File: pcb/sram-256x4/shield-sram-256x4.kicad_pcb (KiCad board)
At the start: 4 copper layers, 100 x 100 mm, 26 parts, among them J1 QSH-060-01-L-D-A, J2 QSH-060-01-L-D-A, U1 IS61WV25616-10TLI, U2 IS61WV25616-10TLI, U3 IS61WV25616-10TLI, U4 IS61WV25616-10TLI

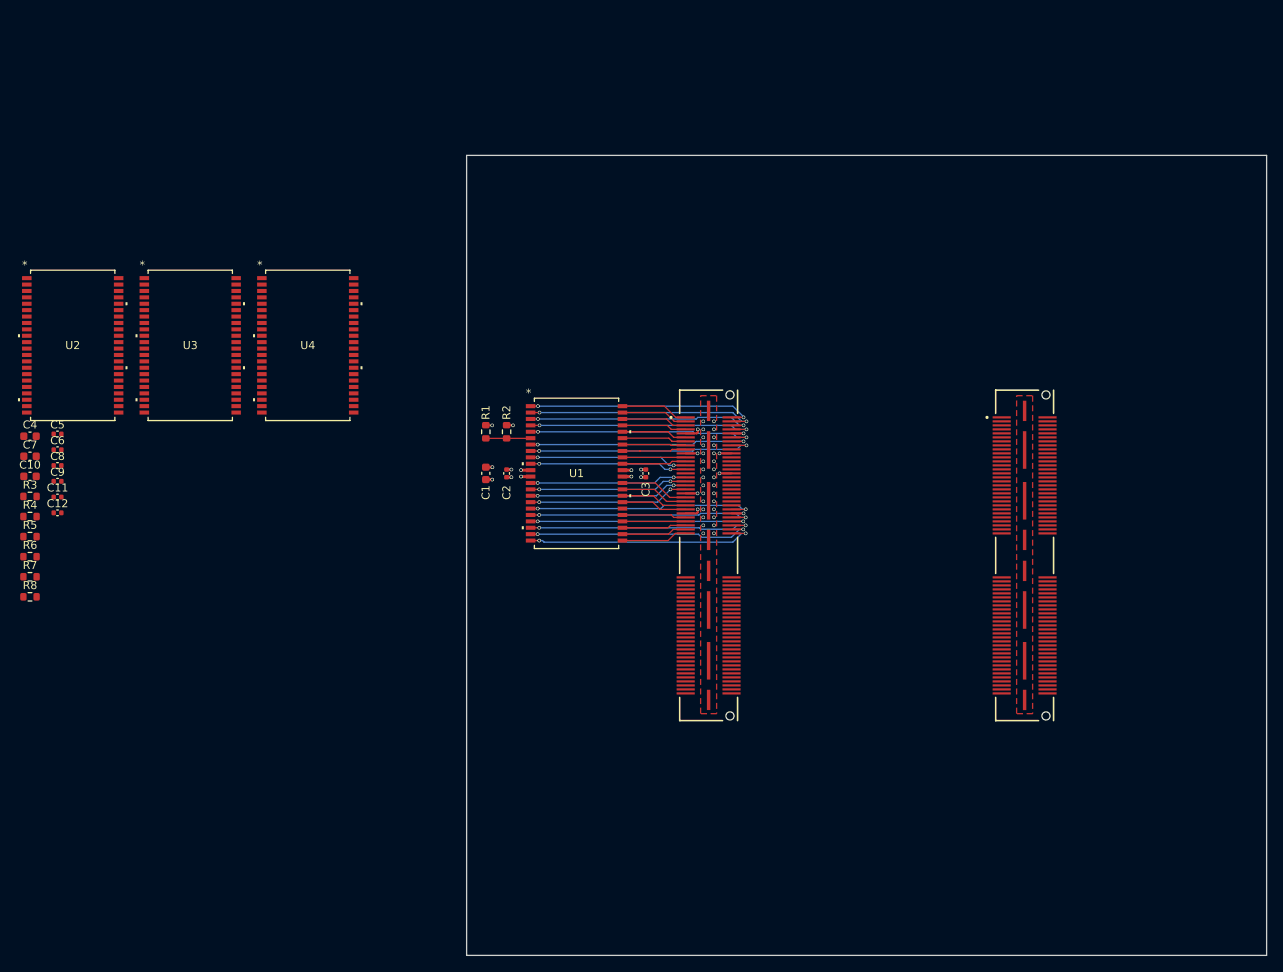
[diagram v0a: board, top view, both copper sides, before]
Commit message: [pcb][sram-4x] all but pmod routed for adc board
The sram is doing double duty here during the cross over. It supports
the dfc stacking connector during the transition. It will be removed.
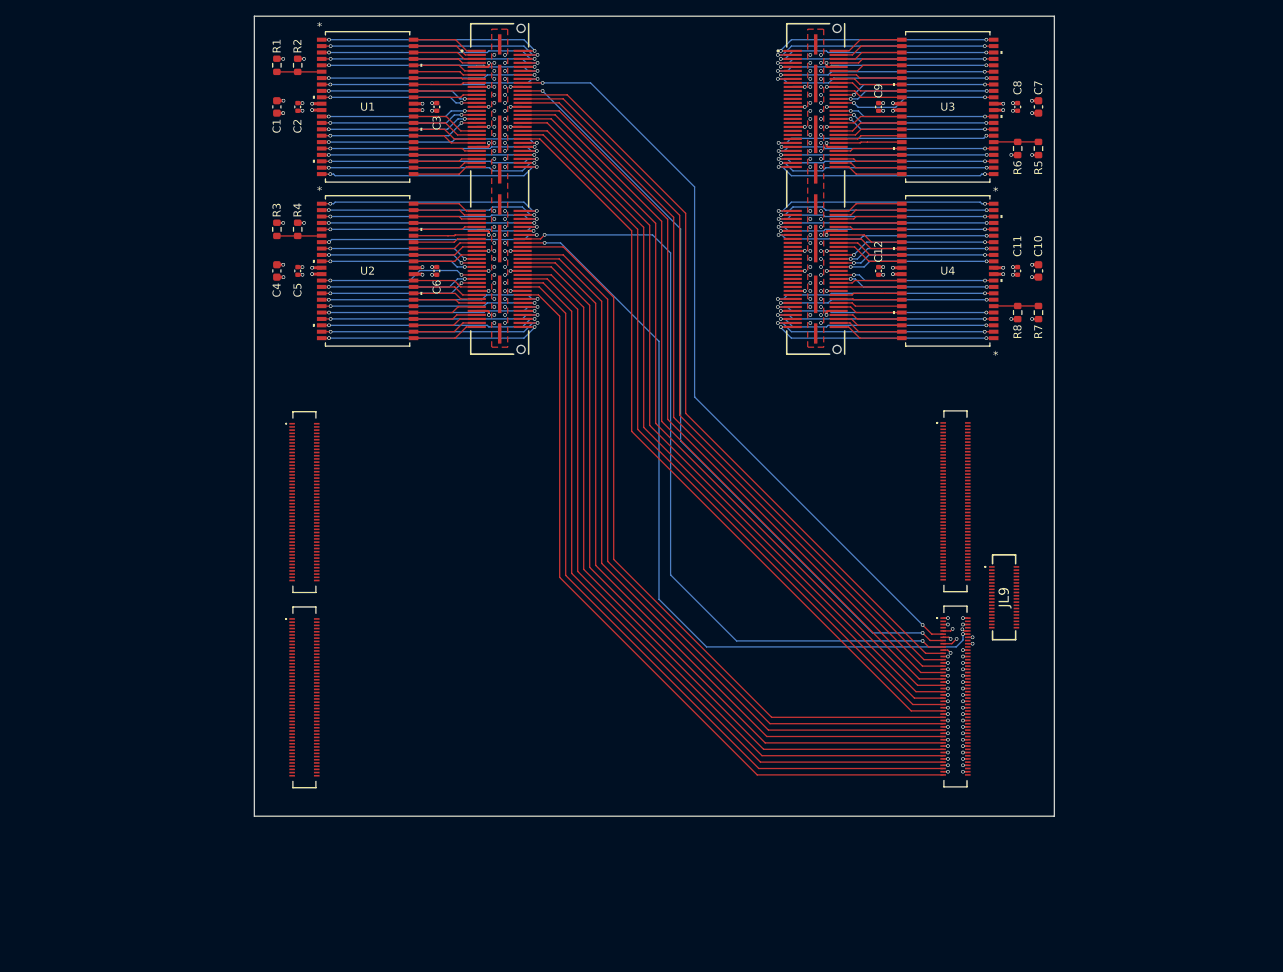
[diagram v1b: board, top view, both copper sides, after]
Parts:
- added JL1: DF40C-100DS-0.4V51, DF40C-100DS-0.4V_51:DF40C100DS04V51, F.Cu at (37.5, 90.9)
- added JL2: DF40C-100DS-0.4V51, DF40C-100DS-0.4V_51:DF40C100DS04V51, F.Cu at (37.5, 115.3)
- added JL3: DF40C-100DS-0.4V51, DF40C-100DS-0.4V_51:DF40C100DS04V51, F.Cu at (118.9, 90.8)
- added JL4: DF40C-100DS-0.4V51, DF40C-100DS-0.4V_51:DF40C100DS04V51, F.Cu at (118.9, 115.2)
- added JL9: DF40C-40DS-0.4V51, DF40C-40DS-0.4V_51:DF40C40DS04V51, F.Cu at (125.0, 102.8)
- moved R5 135.1 mm to (129.3, 46.7), turned to 90 degrees
- moved R6 133.6 mm to (126.7, 46.7), turned to 90 degrees
- moved C7 133.4 mm to (129.3, 41.5), turned to 90 degrees
- moved R7 130.3 mm to (129.3, 67.2), turned to 90 degrees
- moved C10 128.6 mm to (129.3, 62.0), turned to 90 degrees
- moved R8 128.5 mm to (126.7, 67.2), turned to 90 degrees
- moved C8 128.1 mm to (126.7, 41.5), turned to 90 degrees
- moved C11 123.3 mm to (126.7, 62.0), turned to 90 degrees
- moved C9 112.8 mm to (109.3, 41.5), turned to -90 degrees
- moved C12 107.0 mm to (109.3, 62.0), turned to -90 degrees
- moved U3 99.3 mm to (117.9, 41.5), turned to 180 degrees
- moved U4 80.5 mm to (117.9, 62.0), turned to 180 degrees
- moved J2 52.7 mm to (101.4, 51.8)
- moved U1 52.7 mm to (45.4, 41.5)
- moved C1 52.7 mm to (34.1, 41.5)
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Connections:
- R6 pad 1: /U3_CEn -> GND
- R6 pad 2: GND -> /U3_CEn
- R8 pad 1: /U4_CEn -> GND
- R8 pad 2: GND -> /U4_CEn
- U2 pad 10: B23 -> B25
- U2 pad 13: B25 -> B27
- U2 pad 14: B27 -> B29
- U2 pad 15: B29 -> B31
- U2 pad 16: B31 -> B38
- U2 pad 35: B15 -> B19
- U2 pad 36: B13 -> B17
- U2 pad 37: B11 -> B15
- U2 pad 38: B9 -> B13
- U2 pad 39: GND -> B11
- U2 pad 40: GND -> B9
- U2 pad 7: B17 -> B12
- U2 pad 8: B19 -> B21
- U2 pad 9: B21 -> B23
- U3 pad 1: unconnected-(U3-A0-Pad1) -> C49
- U3 pad 10: unconnected-(U3-I/O3-Pad10) -> C26
- U3 pad 13: unconnected-(U3-I/O4-Pad13) -> C24
- U3 pad 14: unconnected-(U3-I/O5-Pad14) -> C22
- U3 pad 15: unconnected-(U3-I/O6-Pad15) -> C20
- U3 pad 16: unconnected-(U3-I/O7-Pad16) -> C13
- U3 pad 17: unconnected-(U3-WE-Pad17) -> C11
- U3 pad 18: unconnected-(U3-A5-Pad18) -> C9
- U3 pad 19: unconnected-(U3-A6-Pad19) -> C7
- U3 pad 2: unconnected-(U3-A1-Pad2) -> C47
- U3 pad 20: unconnected-(U3-A7-Pad20) -> C5
- U3 pad 21: unconnected-(U3-A8-Pad21) -> C3
- U3 pad 22: unconnected-(U3-A9-Pad22) -> C1
- U3 pad 23: unconnected-(U3-A10-Pad23) -> C2
- U3 pad 24: unconnected-(U3-A11-Pad24) -> C4
- U3 pad 25: unconnected-(U3-A12-Pad25) -> C6
- U3 pad 26: unconnected-(U3-A13-Pad26) -> C8
- U3 pad 27: unconnected-(U3-A14-Pad27) -> C10
- U3 pad 29: unconnected-(U3-I/O8-Pad29) -> C12
- U3 pad 3: unconnected-(U3-A2-Pad3) -> C45
- U3 pad 30: unconnected-(U3-I/O9-Pad30) -> C14
- U3 pad 31: unconnected-(U3-I/O10-Pad31) -> C16
- U3 pad 32: unconnected-(U3-I/O11-Pad32) -> C18
- U3 pad 35: unconnected-(U3-I/O12-Pad35) -> C32
- U3 pad 36: unconnected-(U3-I/O13-Pad36) -> C34
- U3 pad 37: unconnected-(U3-I/O14-Pad37) -> C36
- U3 pad 38: unconnected-(U3-I/O15-Pad38) -> C38
- U3 pad 39: GND -> C40
- U3 pad 4: unconnected-(U3-A3-Pad4) -> C43
- U3 pad 40: GND -> C42
- U3 pad 41: unconnected-(U3-OE-Pad41) -> C44
- U3 pad 42: unconnected-(U3-A15-Pad42) -> C46
- U3 pad 43: unconnected-(U3-A16-Pad43) -> C48
- U3 pad 44: unconnected-(U3-A17-Pad44) -> C50
- U3 pad 5: unconnected-(U3-A4-Pad5) -> C41
- U3 pad 7: unconnected-(U3-I/O0-Pad7) -> C39
- U3 pad 8: unconnected-(U3-I/O1-Pad8) -> C30
- U3 pad 9: unconnected-(U3-I/O2-Pad9) -> C28
- U4 pad 1: unconnected-(U4-A0-Pad1) -> D49
- U4 pad 10: unconnected-(U4-I/O3-Pad10) -> D28
- U4 pad 13: unconnected-(U4-I/O4-Pad13) -> D26
- U4 pad 14: unconnected-(U4-I/O5-Pad14) -> D24
- U4 pad 15: unconnected-(U4-I/O6-Pad15) -> D22
- U4 pad 16: unconnected-(U4-I/O7-Pad16) -> D20
- U4 pad 17: unconnected-(U4-WE-Pad17) -> D11
- U4 pad 18: unconnected-(U4-A5-Pad18) -> D9
- U4 pad 19: unconnected-(U4-A6-Pad19) -> D7
- U4 pad 2: unconnected-(U4-A1-Pad2) -> D47
- U4 pad 20: unconnected-(U4-A7-Pad20) -> D5
- U4 pad 21: unconnected-(U4-A8-Pad21) -> D3
- U4 pad 22: unconnected-(U4-A9-Pad22) -> D1
- U4 pad 23: unconnected-(U4-A10-Pad23) -> D2
- U4 pad 24: unconnected-(U4-A11-Pad24) -> D4
- U4 pad 25: unconnected-(U4-A12-Pad25) -> D6
- U4 pad 26: unconnected-(U4-A13-Pad26) -> D8
- U4 pad 27: unconnected-(U4-A14-Pad27) -> D10
- U4 pad 29: unconnected-(U4-I/O8-Pad29) -> D12
- U4 pad 3: unconnected-(U4-A2-Pad3) -> D45
- U4 pad 30: unconnected-(U4-I/O9-Pad30) -> D14
- U4 pad 31: unconnected-(U4-I/O10-Pad31) -> D16
- U4 pad 32: unconnected-(U4-I/O11-Pad32) -> D18
- U4 pad 35: unconnected-(U4-I/O12-Pad35) -> D32
- U4 pad 36: unconnected-(U4-I/O13-Pad36) -> D34
- U4 pad 37: unconnected-(U4-I/O14-Pad37) -> D36
- U4 pad 38: unconnected-(U4-I/O15-Pad38) -> D38
- U4 pad 39: GND -> D40
- U4 pad 4: unconnected-(U4-A3-Pad4) -> D43
- U4 pad 40: GND -> D42
- U4 pad 41: unconnected-(U4-OE-Pad41) -> D44
- U4 pad 42: unconnected-(U4-A15-Pad42) -> D46
- U4 pad 43: unconnected-(U4-A16-Pad43) -> D48
- U4 pad 44: unconnected-(U4-A17-Pad44) -> D50
- U4 pad 5: unconnected-(U4-A4-Pad5) -> D41
- U4 pad 7: unconnected-(U4-I/O0-Pad7) -> D39
- U4 pad 8: unconnected-(U4-I/O1-Pad8) -> D37
- U4 pad 9: unconnected-(U4-I/O2-Pad9) -> D30
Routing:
- net B14: track 0.00 -> 97.7 mm, vias 0 -> 2
- net A38: track 0.00 -> 96.9 mm
- net A36: track 0.00 -> 96.7 mm
- net B34: track 0.00 -> 96.7 mm
- net A32: track 0.00 -> 96.7 mm
- net A34: track 0.00 -> 96.6 mm
- net B32: track 0.00 -> 96.6 mm
- net B16: track 0.00 -> 96.6 mm, vias 0 -> 2
- net A18: track 0.00 -> 96.5 mm, vias 0 -> 2
- net B36: track 0.00 -> 96.5 mm
- net A30: track 0.00 -> 96.5 mm
- net A16: track 0.00 -> 96.5 mm, vias 0 -> 2
- net B30: track 0.00 -> 96.4 mm
- net A28: track 0.00 -> 96.4 mm
- net B26: track 0.00 -> 96.4 mm
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
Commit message: [pcb][sram-4x] fully routed
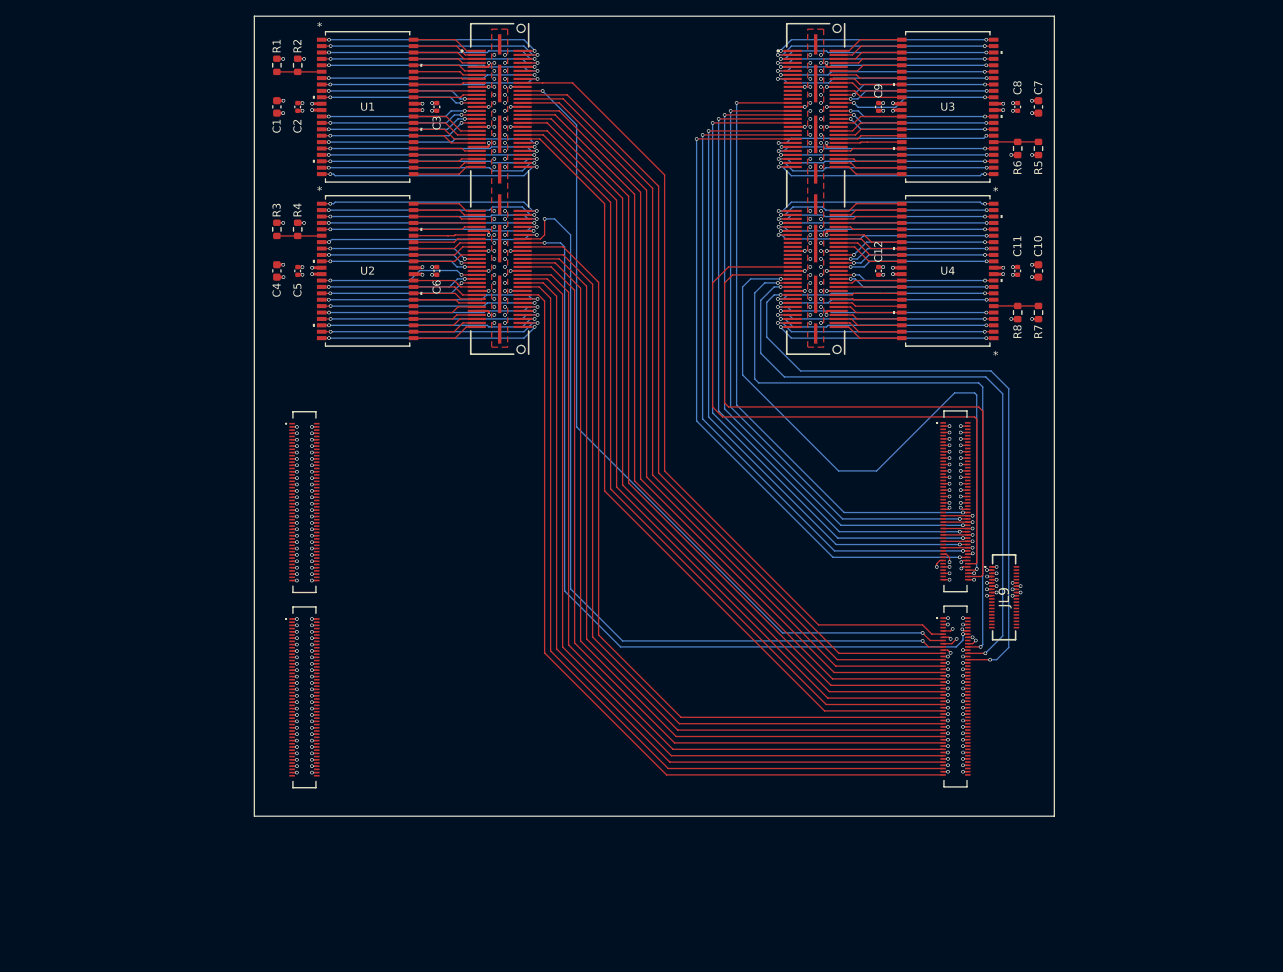
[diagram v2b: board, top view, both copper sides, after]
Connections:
- JL3 pad 58: C_58 -> C23
- JL3 pad 62: C_62 -> C25
- JL3 pad 66: C_66 -> C27
- JL3 pad 70: C_70 -> C29
- JL3 pad 74: C_74 -> C31
- JL3 pad 78: C_78 -> C33
- JL3 pad 82: C_82 -> C35
- JL3 pad 86: C_86 -> C37
- JL3 pad 90: C_90 -> D25
- JL3 pad 94: C_94 -> D29
- JL3 pad 98: C_98 -> D27
- JL4 pad 20: D_20 -> D31
- JL4 pad 24: D_24 -> D33
- JL4 pad 28: D_28 -> D35
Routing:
- net GND: track 53.7 -> 174.9 mm, vias 194 -> 348
- net C37: track 0.00 -> 88.2 mm, vias 0 -> 2
- net C35: track 0.00 -> 86.8 mm, vias 0 -> 2
- net C33: track 0.00 -> 85.3 mm, vias 0 -> 2
- net C31: track 0.00 -> 84.6 mm, vias 0 -> 2
- net C29: track 0.00 -> 83.2 mm, vias 0 -> 2
- net C27: track 0.00 -> 81.7 mm, vias 0 -> 2
- net C25: track 0.00 -> 80.2 mm, vias 0 -> 2
- net C23: track 0.00 -> 79.2 mm, vias 0 -> 2
- net D33: track 0.00 -> 79.2 mm, vias 0 -> 2
- net D25: track 0.00 -> 79.1 mm
- net D31: track 0.00 -> 79.1 mm, vias 0 -> 2
- net D27: track 0.00 -> 79.1 mm
- net D35: track 0.00 -> 79.0 mm, vias 0 -> 2
- net D29: track 0.00 -> 79.0 mm, vias 0 -> 2
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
